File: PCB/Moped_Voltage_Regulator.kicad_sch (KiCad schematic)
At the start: 15 parts, among them J1 Screw_Terminal_01x02, J2 Screw_Terminal_01x02, Q1 IRLZ44N, Q2 IRLZ44N

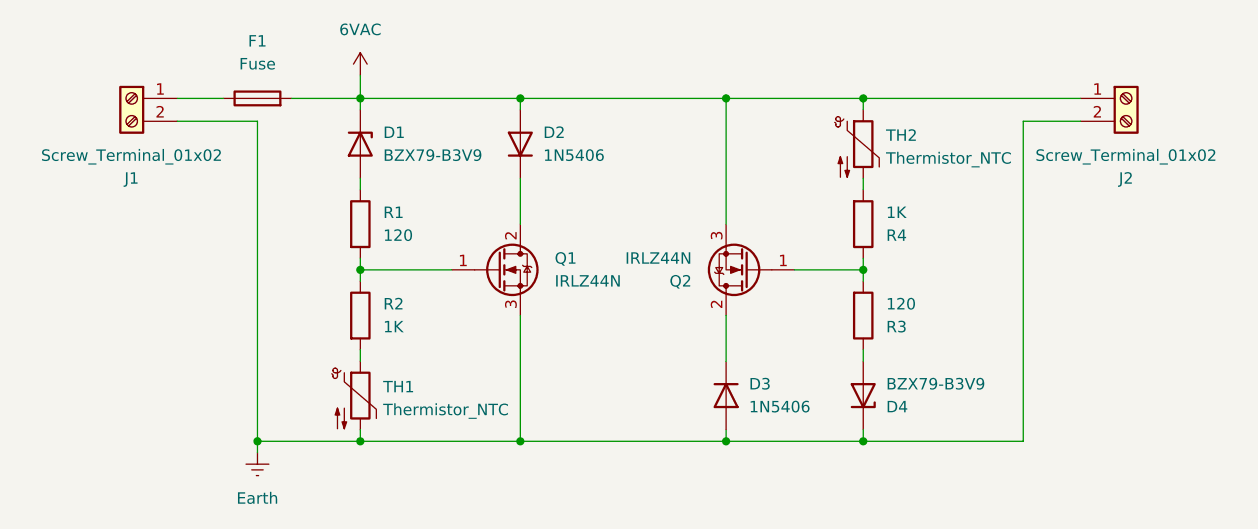
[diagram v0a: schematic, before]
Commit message: Updated schematic and PCB
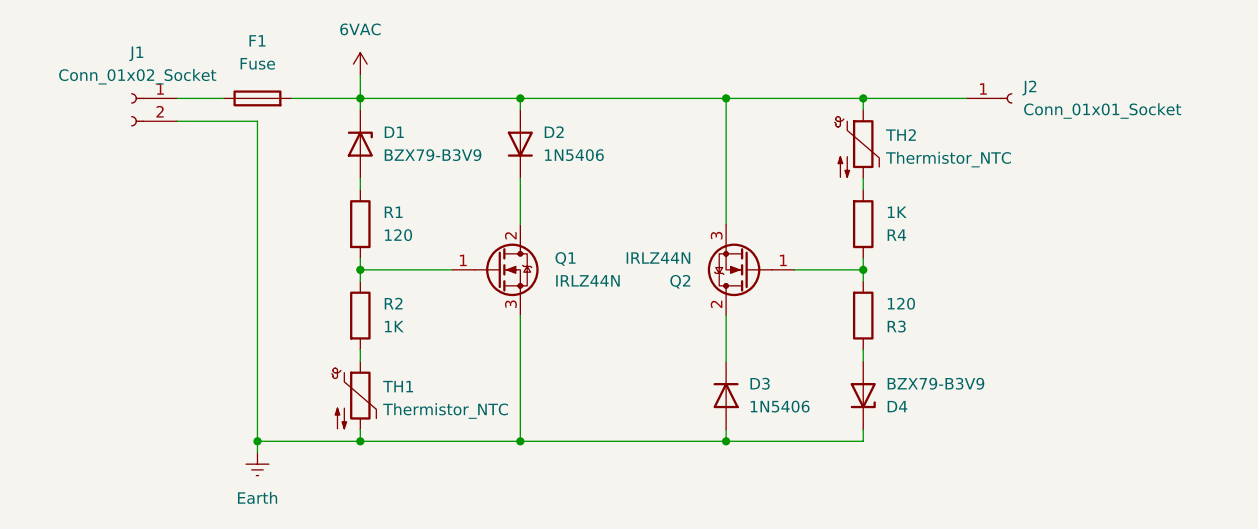
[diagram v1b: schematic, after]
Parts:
- removed J1, J2: Screw_Terminal_01x02, TerminalBlock:TerminalBlock_bornier-2_P5.08mm, symbol Connector:Screw_Terminal_01x02
- added J1: Conn_01x02_Socket, Connector_Wire:SolderWire-0.75sqmm_1x02_P4.8mm_D1.25mm_OD2.3mm, symbol Connector:Conn_01x02_Socket
- added J2: Conn_01x01_Socket, Connector_Wire:SolderWire-0.75sqmm_1x01_D1.25mm_OD2.3mm, symbol Connector:Conn_01x01_Socket
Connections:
- net 6VAC: now also J2.1 (Pin_1)
- net Earth: now also J1.2 (Pin_2)
- net at F1.1: now also J1.1 (Pin_1)
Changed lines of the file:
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@@
 		(color 0 0 0 0)
 	)
-	(junction
-		(at 186.69 115.57)
-		(diameter 0)
-		(color 0 0 0 0)
-	)
 	(wire
 		(pts
@@
 	(wire
 		(pts
-			(xy 210.82 80.01) (xy 204.47 80.01)
-		)
-		(stroke
-			(width 0)
-			(type default)
-		)
-	)
-	(wire
-		(pts
 			(xy 123.19 77.47) (xy 130.81 77.47)
 		)
@@
 	(wire
 		(pts
-			(xy 186.69 77.47) (xy 210.82 77.47)
+			(xy 186.69 77.47) (xy 198.12 77.47)
 		)
 		(stroke
@@
 	(wire
 		(pts
-			(xy 204.47 115.57) (xy 186.69 115.57)
-		)
-		(stroke
-			(width 0)
-			(type default)
-		)
-	)
-	(wire
-		(pts
 			(xy 186.69 114.3) (xy 186.69 115.57)
 		)
@@
 		(pts
 			(xy 179.07 96.52) (xy 186.69 96.52)
-		)
-		(stroke
-			(width 0)
-			(type default)
-		)
-	)
-	(wire
-		(pts
-			(xy 204.47 80.01) (xy 204.47 115.57)
 		)
 		(stroke
@@
 	)
 	(symbol
-		(lib_id "Connector:Screw_Terminal_01x02")
+		(lib_id "Connector:Conn_01x02_Socket")
 		(at 105.41 77.47 0)
 		(mirror y)
@@
 		(on_board yes)
 		(dnp no)
+		(fields_autoplaced yes)
 		(property "Reference" "J1"
-			(at 105.41 86.36 0)
-			(effects
-				(font
-					(size 1.27 1.27)
-				)
-			)
-		)
-		(property "Value" "Screw_Terminal_01x02"
-			(at 105.41 83.82 0)
-			(effects
-				(font
-					(size 1.27 1.27)
-				)
-			)
-		)
-		(property "Footprint" "TerminalBlock:TerminalBlock_bornier-2_P5.08mm"
+			(at 106.045 72.39 0)
+			(effects
+				(font
+					(size 1.27 1.27)
+				)
+			)
+		)
+		(property "Value" "Conn_01x02_Socket"
+			(at 106.045 74.93 0)
+			(effects
+				(font
+					(size 1.27 1.27)
+				)
+			)
+		)
+		(property "Footprint" "Connector_Wire:SolderWire-0.75sqmm_1x02_P4.8mm_D1.25mm_OD2.3mm"
 			(at 105.41 77.47 0)
 			(effects
@@
 			)
 		)
-		(property "Description" "Generic screw terminal, single row, 01x02, script generated (kicad-library-utils/schlib/autogen/connector/)"
+		(property "Description" "Generic connector, single row, 01x02, script generated"
 			(at 105.41 77.47 0)
 			(effects
@@
 			)
 		)
-		(pin "1"
-		)
 		(pin "2"
+		)
+		(pin "1"
 		)
 		(instances
@@
 	)
 	(symbol
+		(lib_id "Connector:Conn_01x01_Socket")
+		(at 203.2 77.47 0)
+		(unit 1)
+		(exclude_from_sim no)
+		(in_bom yes)
+		(on_board yes)
+		(dnp no)
+		(fields_autoplaced yes)
+		(property "Reference" "J2"
+			(at 204.47 76.1999 0)
+			(effects
+				(font
+					(size 1.27 1.27)
+				)
+				(justify left)
+			)
+		)
+		(property "Value" "Conn_01x01_Socket"
+			(at 204.47 78.7399 0)
+			(effects
+				(font
+					(size 1.27 1.27)
+				)
+				(justify left)
+			)
+		)
+		(property "Footprint" "Connector_Wire:SolderWire-0.75sqmm_1x01_D1.25mm_OD2.3mm"
+			(at 203.2 77.47 0)
+			(effects
+				(font
+					(size 1.27 1.27)
+				)
+				(hide yes)
+			)
+		)
+		(property "Datasheet" "~"
+			(at 203.2 77.47 0)
+			(effects
+				(font
+					(size 1.27 1.27)
+				)
+				(hide yes)
+			)
+		)
+		(property "Description" "Generic connector, single row, 01x01, script generated"
+			(at 203.2 77.47 0)
+			(effects
+				(font
+					(size 1.27 1.27)
+				)
+				(hide yes)
+			)
+		)
+		(pin "1"
+		)
+		(instances
+			(project "Moped_Voltage_Regulator"
+				(path "/cd224f18-4e7a-486b-b9a3-5d1abd3b9fbb"
+					(reference "J2")
+					(unit 1)
+				)
+			)
+		)
+	)
+	(symbol
 		(lib_id "Device:D_Zener")
 		(at 186.69 110.49 270)
@@
 					(unit 1)
 				)
-			)
-		)
-	)
-	(symbol
-		(lib_id "Connector:Screw_Terminal_01x02")
-		(at 215.9 77.47 0)
-		(unit 1)
-		(exclude_from_sim no)
-		(in_bom yes)
-		(on_board yes)
-		(dnp no)
-		(property "Reference" "J2"
-			(at 215.9 86.36 0)
-			(effects
-				(font
-					(size 1.27 1.27)
-				)
-			)
-		)
-		(property "Value" "Screw_Terminal_01x02"
-			(at 215.9 83.82 0)
-			(effects
-				(font
-					(size 1.27 1.27)
-				)
-			)
-		)
-		(property "Footprint" "TerminalBlock:TerminalBlock_bornier-2_P5.08mm"
-			(at 215.9 77.47 0)
-			(effects
-				(font
-					(size 1.27 1.27)
-				)
-				(hide yes)
-			)
-		)
-		(property "Datasheet" "~"
-			(at 215.9 77.47 0)
-			(effects
-				(font
-					(size 1.27 1.27)
-				)
-				(hide yes)
-			)
-		)
-		(property "Description" "Generic screw terminal, single row, 01x02, script generated (kicad-library-utils/schlib/autogen/connector/)"
-			(at 215.9 77.47 0)
-			(effects
-				(font
-					(size 1.27 1.27)
-				)
-				(hide yes)
-			)
-		)
-		(pin "1"
-		)
-		(pin "2"
-		)
-		(instances
-			(project "Moped_Voltage_Regulator"
-				(path "/cd224f18-4e7a-486b-b9a3-5d1abd3b9fbb"
-					(reference "J2")
-					(unit 1)
-				)
